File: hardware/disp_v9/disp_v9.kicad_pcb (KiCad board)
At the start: 2 copper layers, 82 x 52 mm, 115 parts, among them J1 Conn_02x16_Odd_Even_FLIP, J2 Conn_01x01_Pin, J3 Conn_01x01_Pin, Q1 2N7002, Q10 2N7002, Q11 2N7002, Q12 2N7002, Q13 2N7002, Q2 2N7002, Q3 2N7002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

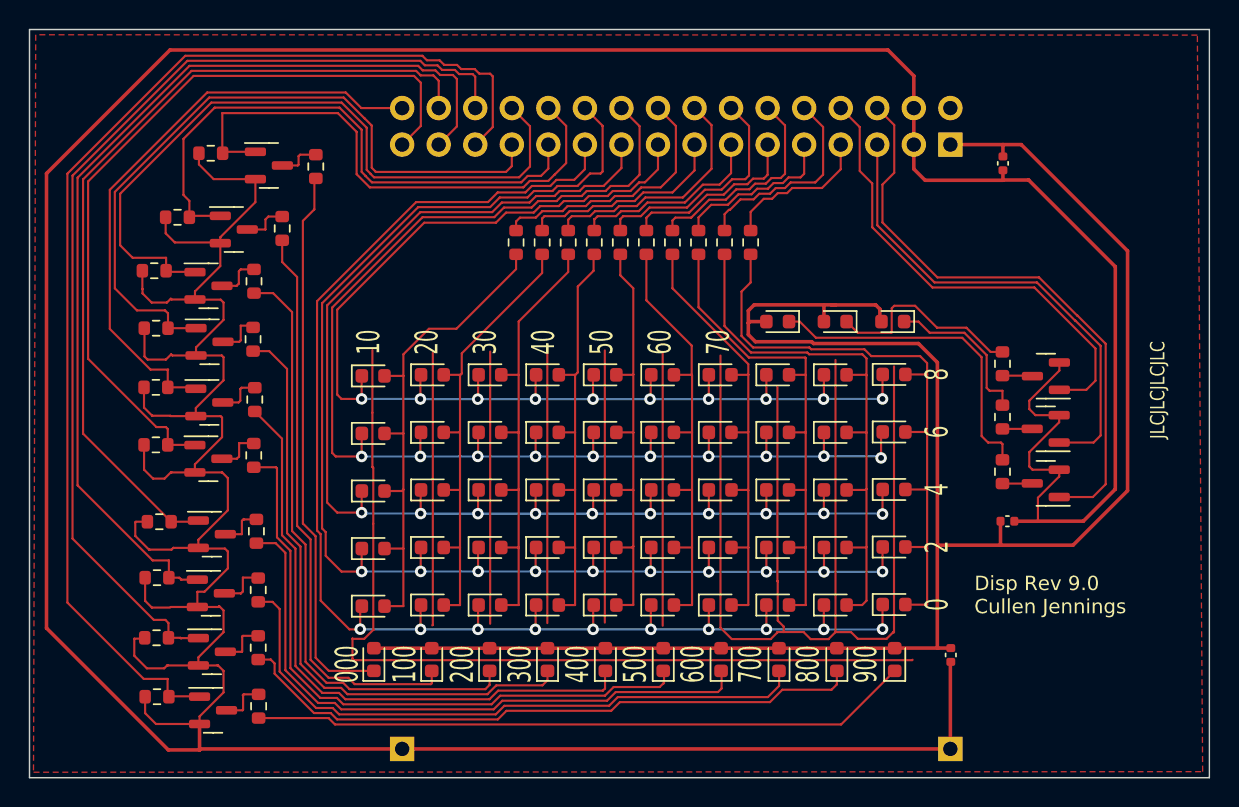
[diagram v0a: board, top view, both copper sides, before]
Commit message: new footprints and symbols for new switch
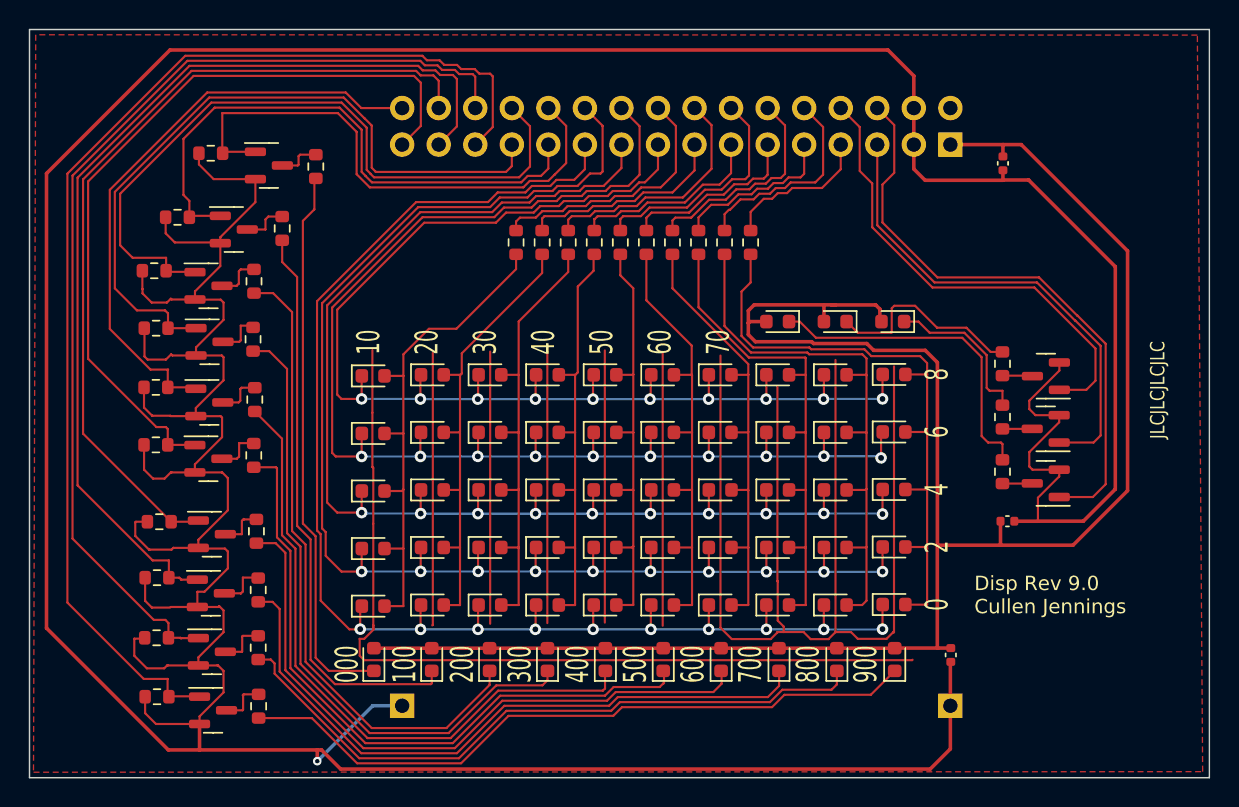
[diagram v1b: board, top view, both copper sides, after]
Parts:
- moved J2 3.00 mm to (233.0, 115.0)
- moved J3 3.00 mm to (194.9, 115.0)
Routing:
- net GND: track 593.0 -> 601.5 mm, vias 0 -> 1
- net /L8: track 42.6 -> 44.8 mm
- net /L3: track 43.9 -> 46.1 mm
- net /L7: track 42.9 -> 45.1 mm
- net /L1: track 45.9 -> 48.2 mm
- net /L2: track 44.3 -> 46.5 mm
- net /L6: track 42.9 -> 45.1 mm
- net /L5: track 44.4 -> 46.7 mm
- net /L4: track 43.7 -> 45.8 mm
